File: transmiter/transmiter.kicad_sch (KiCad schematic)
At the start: 56 parts, among them J1 USB_B_Mini, J2 Conn_01x04_Pin, J3 Conn_01x04_Pin, SW1 SW_Push, SW2 SW_SPDT, U2 STM32F303K8Tx, U3 AMS1117-3.3, Y1 16MHz

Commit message: First stage of PCB design
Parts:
- removed U1, U4: ~, Package_TO_SOT_SMD:SOT-23-5_HandSoldering, symbol communication_circuit:FIN1001M5X
- removed U5: ~, Package_CSP:LFCSP-24-1EP_4x4mm_P0.5mm_EP2.3x2.3mm, symbol communication_circuit:ADL5370
- removed U6: ~, symbol communication_circuit:ADL5531
- removed U7: ~, symbol communication_circuit:crystal
- added AE2: Antenna_Shield, Connector_Coaxial:U.FL_Hirose_U.FL-R-SMT-1_Vertical, symbol Device:Antenna_Shield
- added C29, C31: 100n, Capacitor_SMD:C_0603_1608Metric_Pad1.08x0.95mm_HandSolder, symbol Device:C
- added C30: 4.7u, Capacitor_SMD:C_0603_1608Metric_Pad1.08x0.95mm_HandSolder, symbol Device:C
- added D2, D3: LED, LED_SMD:LED_0805_2012Metric_Pad1.15x1.40mm_HandSolder, symbol Device:LED
- added R10: 1k5, Resistor_SMD:R_0603_1608Metric_Pad0.98x0.95mm_HandSolder, symbol Device:R
- added U1: ADL5370, Package_CSP:LFCSP-24-1EP_4x4mm_P0.5mm_EP2.3x2.3mm, symbol Communication_circuit:ADL5370
- added U4: ADL5531, Package_CSP:LFCSP-8-1EP_3x3mm_P0.5mm_EP1.45x1.74mm, symbol Communication_circuit:ADL5531
- added U5: Si590, Oscillator:Oscillator_SMD_IDT_JU6-6_7.0x5.0mm_P2.54mm, symbol Communication_circuit:Si590
- added U6, U7: FIN1001M5X, Package_TO_SOT_SMD:SOT-23-5_HandSoldering, symbol Communication_circuit:FIN1001M5X
- added U9: FT232RL, Package_SO:SSOP-28_5.3x10.2mm_P0.65mm, symbol Interface_USB:FT232RL
- C13, C14, C4, C6: value 1.1n -> 33p
- C15, C16, C17, C18, C19, C20, C21, C23, C24, C27: footprint Capacitor_SMD:C_0603_1608Metric_Pad1.08x0.95mm_HandSolder -> Capacitor_SMD:C_0402_1005Metric_Pad0.74x0.62mm_HandSolder
- J1: footprint Connector_USB:USB_B_Lumberg_2411_02_Horizontal -> Connector_USB:USB_Mini-B_Lumberg_2486_01_Horizontal
- L1, L2, L3, L4: value 2.7n -> 80u
- L5: footprint Inductor_SMD:L_0603_1608Metric_Pad1.05x0.95mm_HandSolder -> Inductor_SMD:L_1008_2520Metric_Pad1.43x2.20mm_HandSolder
- R4: value 10k -> 1k5
- SW1: footprint (none) -> Communication_circuit:PUSH
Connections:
- net LOIN is gone; now on net GND: C16.2
- net +3V3: now also C29.2, C30.2, R10.1, U5.2 (OC), U5.6 (VDD), U6.1 (VCC), U7.1 (VCC), U9.20 (VCC)
- net DAC1_OUT1: now also U6.5 (D_IN)
- net DAC1_OUT2: now also U7.5 (D_IN)
- net GND: now also C9.1, AE2.2 (Shield), C29.1, C30.1, C31.1, U1.1 (COM1), U1.10 (COM2), U1.11 (COM3), U1.12 (COM3), U1.2 (COM1), U1.21 (COM4), U1.22 (COM4), U1.25 (EPAD), U1.7 (COM2), U4.9 (EPAD), U5.3 (GND), U6.2 (GND), U7.2 (GND), U9.18 (GND), U9.21 (GND), U9.25 (AGND), U9.26 (TEST), U9.7 (GND); no longer C9.2
- net IBBN: now also U1.20 (IBBN)
- net IBBP: now also U1.19 (IBBP)
- net LOIP: now also U5.4 (CLK_P)
- net QBBN: now also U1.23 (QBBN)
- net QBBP: now also U1.24 (QBBP)
- net RF_OUT: now also U1.13 (VOUT)
- net USART1_RX: now also U9.1 (TXD)
- net USART1_TX: now also U9.5 (RXD)
- net USB_D+: now also U9.15 (USBD+); no longer R4.2
- net USB_D-: now also U9.16 (USBD-)
- net at C13.1, L3.1, R6.1: now also U7.3 (D_OUT-)
- net at C13.2, L4.1, R7.2: now also U7.4 (D_OUT+)
- net at C4.2, L2.1, R3.2: now also U6.4 (D_OUT+)
- net at C26.1, L5.2: now also U4.7 (RFOUT)
- net at C16.1: now also U1.9 (LOIN)
- net at C4.1, L1.1, R2.1: now also U6.3 (D_OUT-)
- net USART1_CTS: now reaches U2.21 (PA11)
- net USART1_CTS: now also U9.3 (RTS)
- net USART1_RTS: now reaches U2.22 (PA12)
- net USART1_RTS: now also U9.11 (CTS)
- net at C15.1: now also U1.8 (LOIP)
- net at C17.2: now also U4.2 (RFIN)
- net at C22.1: now also U4.5 (CLIN)
- net RF_OUT_AMPLIFIED: no longer names the net of C26.2
- net RF_OUT_AMPLIFIED: now also AE2.1 (A)
- net VBUS renamed +5V
- net +5V: now also C9.2, U1.14 (VPS2), U1.15 (VPS2), U1.16 (VPS3), U1.17 (VPS4), U1.18 (VPS5), U1.3 (VPS1), U1.4 (VPS1), U1.5 (VPS1), U1.6 (VPS1); no longer C9.1
- new net: D3.2 (A), R10.2
- new net: D2.2 (A), R4.2
- new net: C31.2, U9.17 (3V3OUT), U9.4 (VCCIO)
- new net RXLED: D2.1 (K), U9.22 (CBUS1)
- new net TXLED: D3.1 (K), U9.23 (CBUS0)
- no-connect marks 24 -> 33
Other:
- note added: "czy tu wgl są potrzebne te kondensatory do 5V??!!"
- note added: "http://tme.eu/pl/details/ds1104-bn0srs/zlacza-usb-i-ieee1394/connfly/"
- note added: "https://botland.com.pl/usb-uart.html"
- note added: "https://www.digikey.in/en/products/detail/530NB433M000DG"
- note added: "https://www.mouser.pl/ADL5370ACPZ-R7"
- note added: "https://www.tme.eu/pl/ft232rl-reel/"
- note removed: "Si530"
- note removed: "https://www.digikey.in/en/products/detail/530NB433M000DG/8696401"
- note removed: "https://www.mouser.pl/ProductDetail/Analog-Devices/ADL5370ACPZ-R7"
- moved on the sheet: C1, C10, C11, C12, C13, C14, C15, C16, C17, C18, C19, C2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

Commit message: Finished PCB design
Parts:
- removed C27: C, Capacitor_SMD:C_0402_1005Metric_Pad0.74x0.62mm_HandSolder, symbol Device:C
- removed U2: STM32F303K8Tx, Package_QFP:LQFP-32_7x7mm_P0.8mm, symbol MCU_ST_STM32F3:STM32F303K8Tx
- removed U5: Si590, Oscillator:Oscillator_SMD_IDT_JU6-6_7.0x5.0mm_P2.54mm, symbol Communication_circuit:Si590
- added C32, C33, C34: C, Capacitor_SMD:C_0603_1608Metric_Pad1.08x0.95mm_HandSolder, symbol Device:C
- added H1, H2, H3, H4: MountingHole_Pad, MountingHole:MountingHole_2.2mm_M2_DIN965_Pad, symbol Mechanical:MountingHole_Pad
- added L6: 18n, Inductor_SMD:L_0603_1608Metric_Pad1.05x0.95mm_HandSolder, symbol Device:L
- added R11: 1.5k, Resistor_SMD:R_0603_1608Metric_Pad0.98x0.95mm_HandSolder, symbol Device:R
- added R12: 1k, Resistor_SMD:R_0603_1608Metric_Pad0.98x0.95mm_HandSolder, symbol Device:R
- added U2: MAX2608, Package_TO_SOT_SMD:SOT-23-6, symbol Communication_circuit:MAX2608
- added U8: STM32F303K8Tx, Package_QFP:LQFP-32_7x7mm_P0.8mm, symbol MCU_ST_STM32F3:STM32F303K8Tx
- AE2: footprint Connector_Coaxial:U.FL_Hirose_U.FL-R-SMT-1_Vertical -> Connector_Coaxial:U.FL_Molex_MCRF_73412-0110_Vertical
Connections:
- net +3V3: now also U8.1 (VDD), U8.17 (VDD); no longer C29.2, C30.2, U9.20 (VCC)
- net +3VA3: now also U8.5 (VDDA)
- net +5V: now also C29.2, C30.2, U9.20 (VCC), C33.2, R12.1, U2.5 (VCC)
- net BOOT: now also U8.31 (BOOT0)
- net DAC1_OUT1: now also U8.10 (PA4)
- net DAC1_OUT2: now also U8.11 (PA5)
- net GND: now also C32.1, C33.1, H1.1, H2.1, H3.1, H4.1, L6.1, U2.3 (GND), U8.16 (VSS), U8.32 (VSS); no longer C16.2
- net HSE_IN: now also U8.2 (PF0)
- net HSE_OUT: now also U8.3 (PF1)
- net LOIP: now also C34.2
- net NRST: now also U8.4 (NRST)
- net SWCLK: now also U8.24 (PA14)
- net SWDIO: now also U8.25 (PA15)
- net USART1_RX: now also U8.20 (PA10)
- net USART1_TX: now also U8.19 (PA9)
- net USB_D+: now also R11.2
- net 3V3: now reaches C31.2, U9.17 (3V3OUT), U9.4 (VCCIO)
- net 3V3: now also R11.1
- net USART1_CTS: no longer names the net of U9.3 (RTS)
- net USART1_RTS: no longer names the net of U9.11 (CTS)
- new net: C32.2, U2.2 (TUNE)
- new net: C34.1, R12.2, U2.6 (OUT+)
- new net: L6.2, U2.1 (IND)
- new net LOIN: C16.2, U2.4 (OUT-)
- no-connect marks 33 -> 35
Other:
- note added: "https://www.digikey.pl/en/products/MAX2608EUT-T"
- note removed: "czy tu wgl są potrzebne te kondensatory do 5V??!!"
- note removed: "https://www.digikey.in/en/products/detail/530NB433M000DG"
- moved on the sheet: C1, C10, C11, C12, C13, C14, C15, C16, C18, C19, C2, C20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

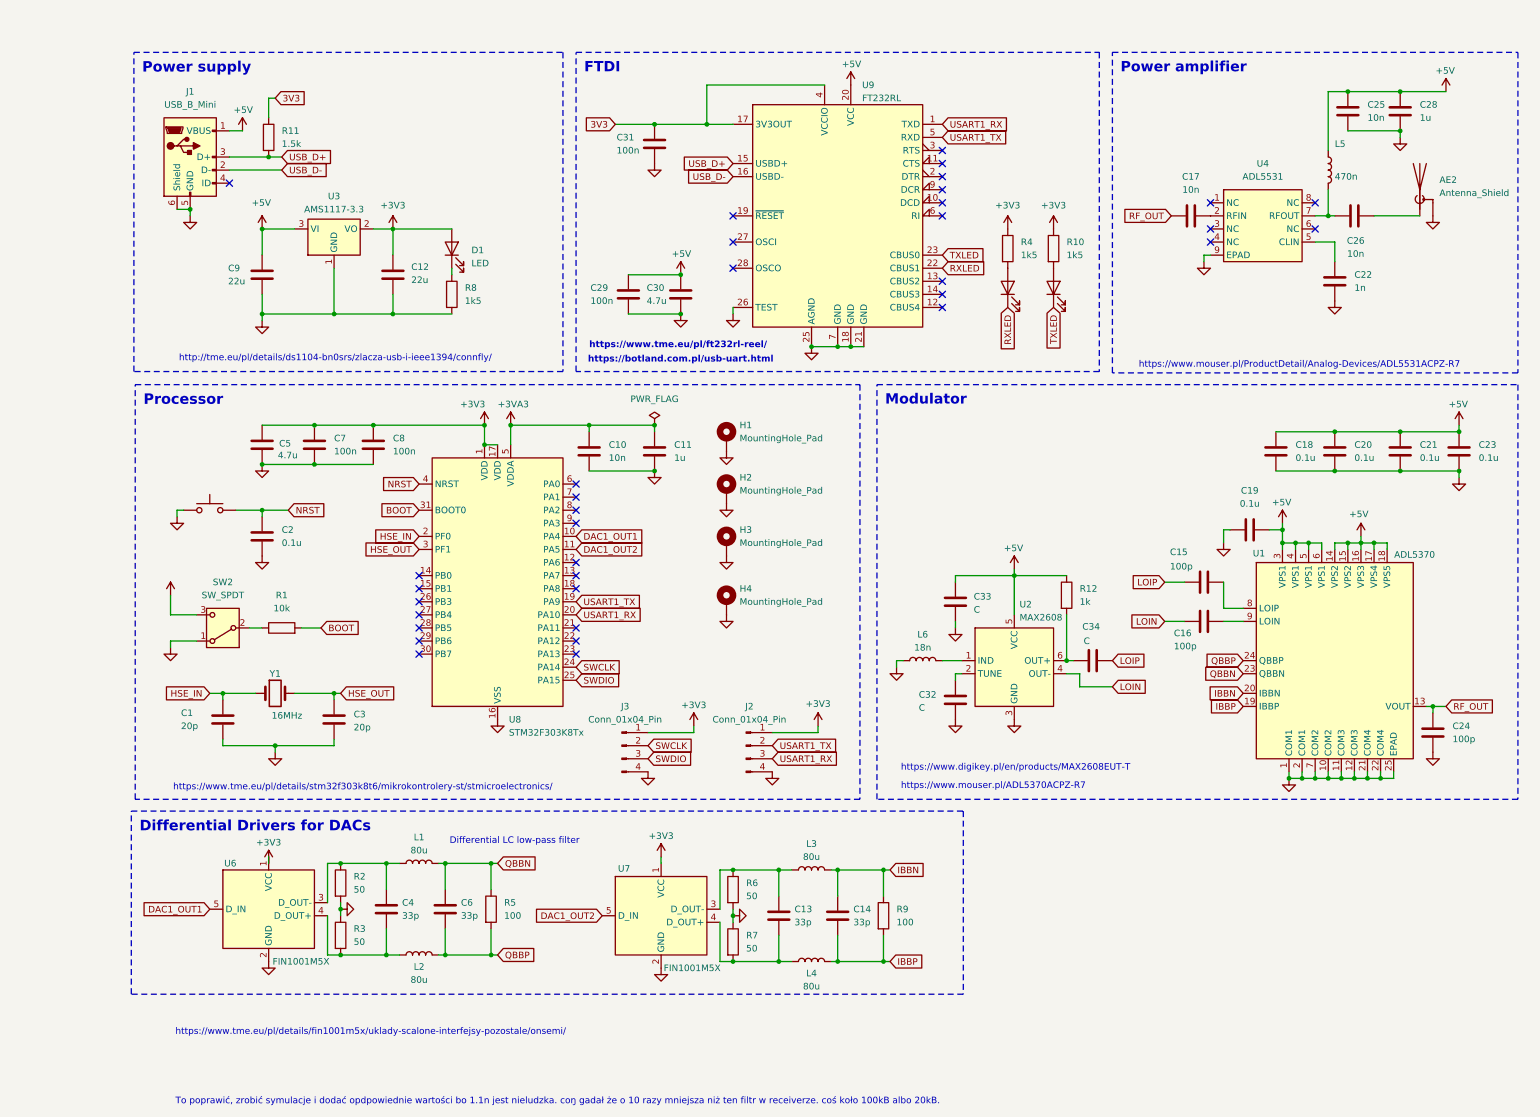
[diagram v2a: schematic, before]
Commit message: First design of sended PCBs
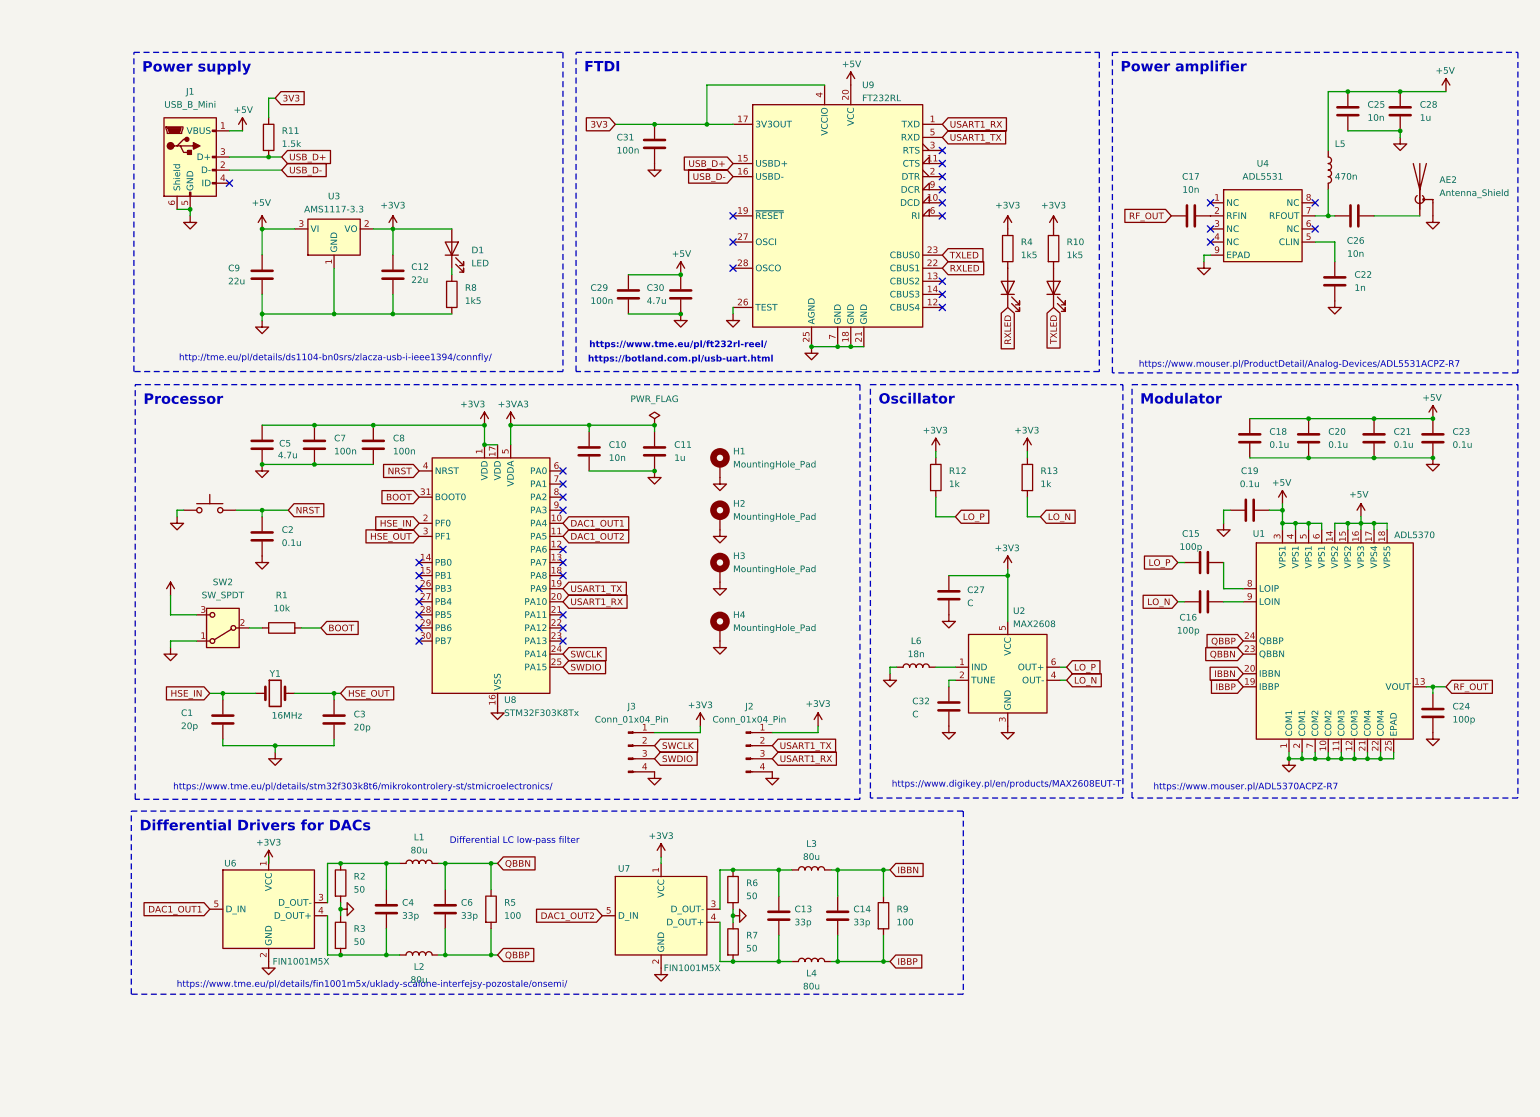
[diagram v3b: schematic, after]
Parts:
- removed C33, C34: C, Capacitor_SMD:C_0603_1608Metric_Pad1.08x0.95mm_HandSolder, symbol Device:C
- added C27: C, Capacitor_SMD:C_0603_1608Metric_Pad1.08x0.95mm_HandSolder, symbol Device:C
- added R13: 1k, Resistor_SMD:R_0603_1608Metric_Pad0.98x0.95mm_HandSolder, symbol Device:R
- C15, C16: footprint Capacitor_SMD:C_0402_1005Metric_Pad0.74x0.62mm_HandSolder -> (none)
- C26: footprint Capacitor_SMD:C_0603_1608Metric_Pad1.08x0.95mm_HandSolder -> Capacitor_SMD:C_0402_1005Metric_Pad0.74x0.62mm_HandSolder
- L1, L2, L3, L4: footprint Inductor_SMD:L_0603_1608Metric_Pad1.05x0.95mm_HandSolder -> Inductor_SMD:L_1210_3225Metric_Pad1.42x2.65mm_HandSolder
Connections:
- net LOIP is gone; now on an unnamed net: C15.2
- net +3V3: now also R12.1, U2.5 (VCC), C27.2, R13.1
- net +5V: no longer R12.1, U2.5 (VCC)
- net GND: now also C27.1
- net LO_P: now reaches R12.2, U2.6 (OUT+)
- net LO_P: now also C15.1
- net at U1.9 (LOIN): now also C16.2; no longer C16.1
- net at U1.8 (LOIP): no longer C15.1
- net LOIN renamed LO_N
- net LO_N: now also C16.1, R13.2; no longer C16.2
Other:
- note removed: "To poprawić, zrobić symulacje i dodać opdpowiednie wartości bo 1.1n jest nieludzka. coŋ gadał że o 10 razy mniejsza niż ten filtr w receiverze. coś koło 100kB albo 20kB."
- moved on the sheet: C18, C19, C20, C21, C23, C24, C32, H1, H2, H3, H4, J3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

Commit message: Correction to PCBs
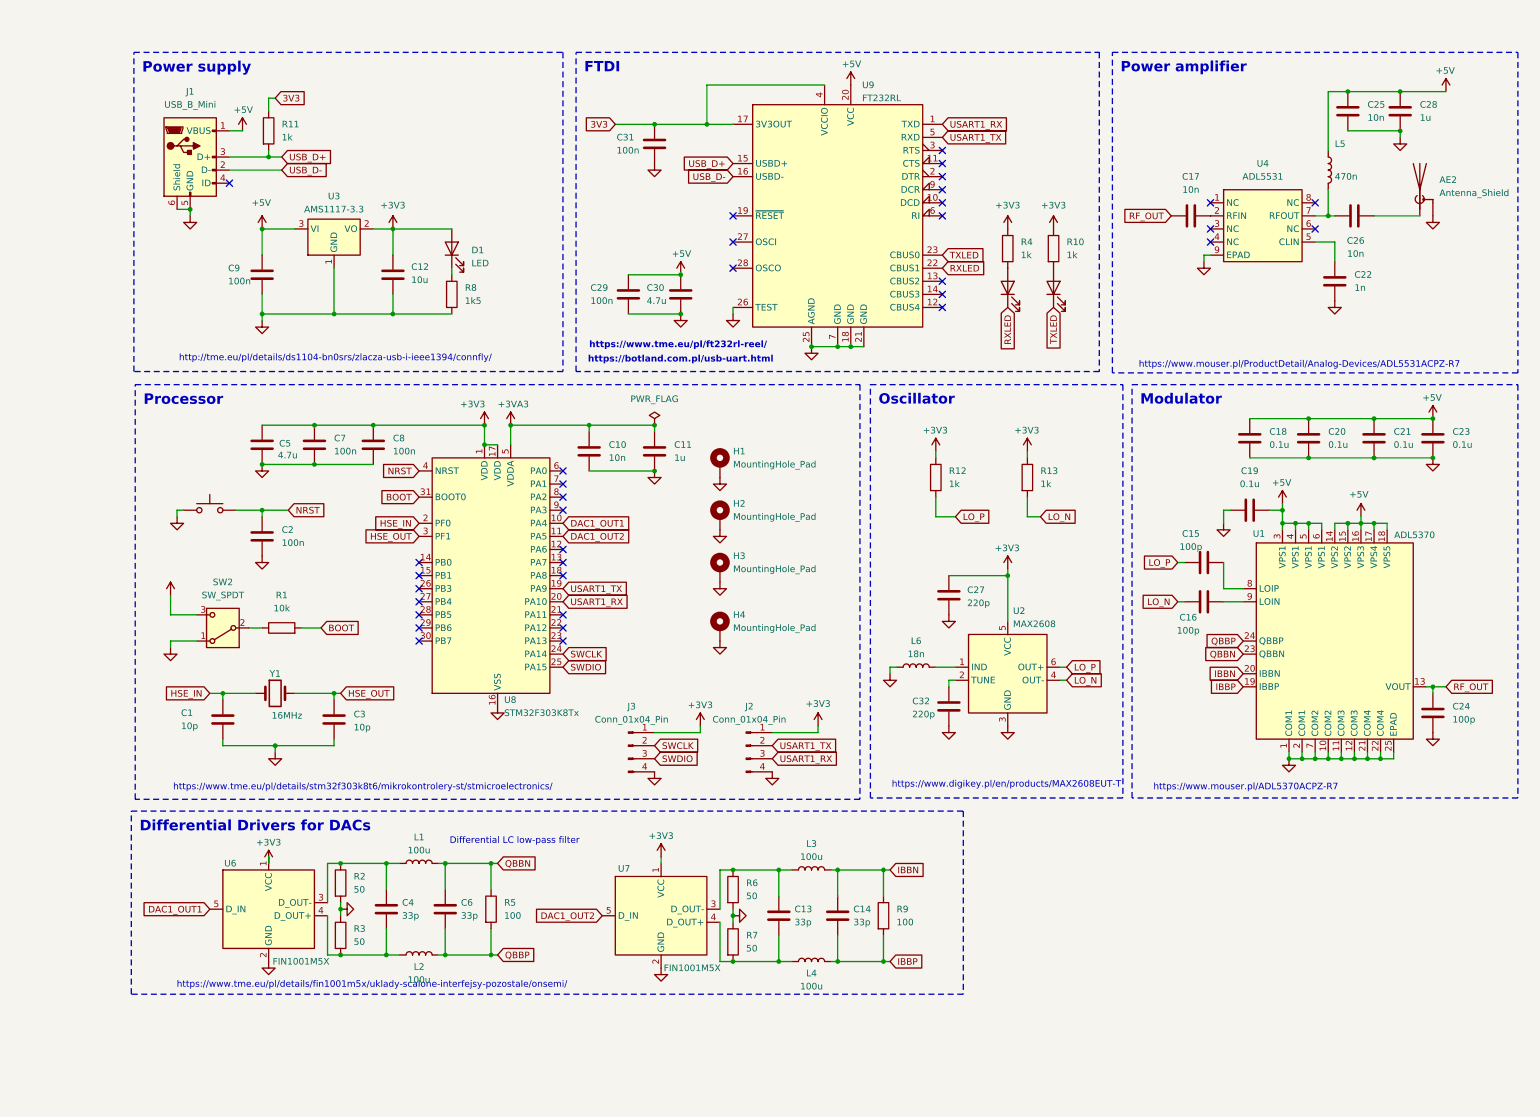
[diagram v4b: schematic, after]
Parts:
- C1, C3: value 20p -> 10p
- C12: value 22u -> 10u
- C15, C16: footprint (none) -> Capacitor_SMD:C_0402_1005Metric_Pad0.74x0.62mm_HandSolder
- C2: value 0.1u -> 100n
- C27, C32: value C -> 220p
- C9: value 22u -> 100n
- L1, L2, L3, L4: value 80u -> 100u
- R10, R4: value 1k5 -> 1k
- R11: value 1.5k -> 1k
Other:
- moved on the sheet: R11
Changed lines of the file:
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@@
 	(wire
 		(pts
-			(xy 40.64 22.86) (xy 40.64 26.67)
+			(xy 40.64 22.86) (xy 40.64 25.4)
 		)
 		(stroke
@@
 	(wire
 		(pts
+			(xy 40.64 33.02) (xy 40.64 34.29)
+		)
+		(stroke
+			(width 0)
+			(type default)
+		)
+	)
+	(wire
+		(pts
 			(xy 74.93 171.45) (xy 83.82 171.45)
 		)
@@
 			)
 		)
-		(property "Footprint" ""
+		(property "Footprint" "Capacitor_SMD:C_0402_1005Metric_Pad0.74x0.62mm_HandSolder"
 			(at 226.06 119.6848 0)
 			(effects
@@
 			)
 		)
-		(property "Value" "1k5"
+		(property "Value" "1k"
 			(at 195.58 53.3399 0)
 			(effects
@@
 			)
 		)
-		(property "Value" "22u"
+		(property "Value" "100n"
 			(at 32.766 58.42 0)
 			(effects
@@
 			)
 		)
-		(property "Footprint" ""
+		(property "Footprint" "Capacitor_SMD:C_0402_1005Metric_Pad0.74x0.62mm_HandSolder"
 			(at 226.06 112.0648 0)
 			(effects
@@
 			)
 		)
-		(property "Value" "C"
+		(property "Value" "220p"
 			(at 165.608 142.494 0)
 			(effects
@@
 			)
 		)
-		(property "Value" "20p"
+		(property "Value" "10p"
 			(at 23.622 144.78 0)
 			(effects
@@
 			)
 		)
-		(property "Value" "80u"
+		(property "Value" "100u"
 			(at 69.85 194.056 90)
 			(effects
@@
 			)
 		)
-		(property "Value" "1k5"
+		(property "Value" "1k"
 			(at 186.69 53.3399 0)
 			(effects
@@
 			)
 		)
-		(property "Value" "80u"
+		(property "Value" "100u"
 			(at 146.05 195.326 90)
 			(effects
@@
 			)
 		)
-		(property "Value" "80u"
+		(property "Value" "100u"
 			(at 146.05 170.18 90)
 			(effects
@@
 			)
 		)
-		(property "Value" "80u"
+		(property "Value" "100u"
 			(at 69.85 168.91 90)
 			(effects
@@
 			)
 		)
-		(property "Value" "20p"
+		(property "Value" "10p"
 			(at 57.15 145.034 0)
 			(effects
@@
 			)
 		)
-		(property "Value" "0.1u"
+		(property "Value" "100n"
 			(at 43.18 109.2199 0)
 			(effects
@@
 			)
 		)
-		(property "Value" "22u"
+		(property "Value" "10u"
 			(at 68.326 58.166 0)
 			(effects
@@
 			)
 		)
-		(property "Value" "C"
+		(property "Value" "220p"
 			(at 176.276 120.904 0)
 			(effects
@@
 	(symbol
 		(lib_id "Device:R")
-		(at 40.64 30.48 0)
+		(at 40.64 29.21 0)
 		(unit 1)
 		(exclude_from_sim no)
@@
 		(fields_autoplaced yes)
 		(property "Reference" "R11"
-			(at 43.18 29.2099 0)
+			(at 43.18 27.9399 0)
 			(effects
 				(font
@@
 			)
 		)
-		(property "Value" "1.5k"
-			(at 43.18 31.7499 0)
+		(property "Value" "1k"
+			(at 43.18 30.4799 0)
 			(effects
 				(font
@@
 		)
 		(property "Footprint" "Resistor_SMD:R_0603_1608Metric_Pad0.98x0.95mm_HandSolder"
-			(at 38.862 30.48 90)
+			(at 38.862 29.21 90)
 			(effects
 				(font
@@
 		)
 		(property "Datasheet" "~"
-			(at 40.64 30.48 0)
+			(at 40.64 29.21 0)
 			(effects
 				(font
@@
 		)
 		(property "Description" "Resistor"
-			(at 40.64 30.48 0)
+			(at 40.64 29.21 0)
 			(effects
 				(font
